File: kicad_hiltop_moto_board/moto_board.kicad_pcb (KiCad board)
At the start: 4 copper layers, 159.9 x 99.9 mm, 421 parts, among them J1 Conn_02x06_Counter_Clockwise, J10 Conn_ARM_JTAG_SWD_10, J2 Conn_02x06_Counter_Clockwise, J3 Conn_03x32_DIN41612, J4 Conn_02x06_Counter_Clockwise, J5 Conn_02x06_Counter_Clockwise, J6 Conn_02x06_Counter_Clockwise, J7 Conn_02x06_Counter_Clockwise, J8 Conn_02x06_Counter_Clockwise, J9 Conn_02x06_Counter_Clockwise, K1 HRS1KH-S, Q10 ZXMN6A07F, Q11 ZXMN6A07F, Q2 ZXMN6A07F, Q7 ZXMN6A07F, Q8 ZXMN6A07F, SW1 SW_Push, SW2 SW_DIP_x04, SW3 SW_DIP_x04, SW4 SW_DIP_x04, SW5 SW_DIP_x04, U1 INA250A4, U10 MAX31865, U11 MAX31865, U13 CP2102N-A01-GQFN24, U14 BTS4140N, U15 BTS4140N, U16 MAX4194, U17 BTS4140N, U18 BTS4140N, U19 MAX4194, U2 LD1117S33TR_SOT223, U20 MAX4194, U21 MAX4194, U22 STM32F072RBTx, U23 MAX4194, U24 MAX4194, U25 MAX4194, U26 MAX4194, U27 USB2502, U3 AT25DN512CSSHF-B, U4 AD8646, U5 AD8646, U6 LM75B, U7 AT24C02C-SSHM-T, U8 MAX31865, U9 MAX31865, Y1 50ppm 24.000MHZ, Y2 8MHZ, Y3 ABS25-32.768KHZ-6-T

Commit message: Started on moto board layout
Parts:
- removed C20, C21, C22, C25: 100nF, Capacitor_SMD:C_0603_1608Metric
- removed C23, C60, C61, C66, C67: 100nF, Capacitor_SMD:C_0402_1005Metric
- removed C26, C28, C29, C31, C32, C34, C36, C37, C39, C42, C44, C45, C47, C50, C53, C54: Ccm, Capacitor_SMD:C_0603_1608Metric
- removed C27, C30, C33, C35, C38, C43, C46, C51: Cdiff, Capacitor_SMD:C_0603_1608Metric
- removed C40, C41, C48, C49, C68, C69, C86, C87: 0.1uF, Capacitor_SMD:C_0402_1005Metric
- removed C57, C58, C63, C64: DNF, Capacitor_SMD:C_0805_2012Metric
- removed D14, D15, D16, D17, D18, D19, D20, D21, D22, D23, D24, D25: BAV99, Package_TO_SOT_SMD:SOT-23
- removed D4: BAT54T1G, Diode_SMD:D_SOD-123
- removed J10: Conn_ARM_JTAG_SWD_10, Connector_PinHeader_2.54mm:PinHeader_2x05_P2.54mm_Vertical
- removed J6, J7, J8, J9: Conn_02x06_Counter_Clockwise, Devtank_PCB_Lib:Molex2x06
- removed K1: HRS1KH-S, Devtank_PCB_Lib:Relay_SPDT_HRS1KH-S
- removed L3, L4, L6, L7: 2A/0.05DCR, Inductor_SMD:L_0805_2012Metric
- removed Q10, Q11: ZXMN6A07F, Package_TO_SOT_SMD:SOT-23
- removed R100, R101, R125, R126, R127, R128, R129, R130, R131, R132, R133, R134, R135, R136, R88, R89: 1K, Resistor_SMD:R_0603_1608Metric
- removed R103, R104, R91, R92: 0R, Resistor_SMD:R_0805_2012Metric
- removed R106, R107, R94, R95: 100K, Resistor_SMD:R_0603_1608Metric
- removed R113, R117, R122, R123, R42, R43, R44, R45, R49, R51, R53, R58, R59, R60, R61, R67, R68, R70, R71: R, Resistor_SMD:R_0603_1608Metric
- removed R114, R115, R116, R118, R119, R36, R62, R63, R73: DNF, Resistor_SMD:R_0603_1608Metric
- removed R149, R41, R46, R47, R66: 0R, Resistor_SMD:R_0603_1608Metric
- removed R35: 100R, Resistor_SMD:R_0603_1608Metric
- removed R37, R38, R52: 10K, Resistor_SMD:R_0603_1608Metric
- removed R48: 2K2, Resistor_SMD:R_0603_1608Metric
- removed R50: 470R, Resistor_SMD:R_0603_1608Metric
- removed R54, R55, R64, R65: 30R, Resistor_SMD:R_0603_1608Metric
- removed R56, R57, R69, R72: 12.4K, Resistor_SMD:R_0603_1608Metric
- removed R85, R86, R97, R98: DNF, Resistor_SMD:R_0805_2012Metric
- removed SW2, SW3, SW4, SW5: SW_DIP_x04, Button_Switch_SMD:SW_DIP_SPSTx04_Slide_Copal_CHS-04B_W7.62mm_P1.27mm
- removed TP100, TP106, TP107, TP24, TP25, TP26, TP27, TP28, TP29, TP30, TP37, TP38, TP39, TP40, TP41, TP42, TP43, TP44, TP45, TP46, TP47, TP48, TP49, TP50, TP51, TP52, TP53, TP54, TP55, TP56, TP57, TP58, TP59, TP60, TP61, TP62, TP63, TP64, TP65, TP66, TP67, TP68, TP69, TP70, TP71, TP72, TP73, TP74, TP75, TP76, TP77, TP78, TP79, TP80, TP81, TP82, TP83, TP84, TP85, TP86, TP87, TP88, TP89, TP90, TP91, TP92, TP93, TP94, TP95, TP96, TP97, TP98, TP99: Test_Point, TestPoint:TestPoint_THTPad_D1.0mm_Drill0.5mm
- removed U10, U11, U8, U9: MAX31865, Package_DFN_QFN:TQFN-20-1EP_5x5mm_P0.65mm_EP3.1x3.1mm
- removed U14, U15, U17, U18: BTS4140N, Package_TO_SOT_SMD:SOT-223
- removed U16, U19, U20, U21, U23, U24, U25, U26: MAX4194, Package_SO:SOIC-8_3.9x4.9mm_P1.27mm
- removed U4, U5: AD8646, Package_SO:SOIC-8_3.9x4.9mm_P1.27mm
- removed U6: LM75B, Package_SO:SOIC-8_3.9x4.9mm_P1.27mm
- added F2: Polyfuse, Fuse:Fuse_2920_7451Metric, F.Cu at (4.80, 83.9)
- added Q1: CSD18540Q5B, Package_SON:VSONP-8-1EP_5x6_P1.27mm, F.Cu at (-28.4, 46.6)
- added Q3: CSD18540Q5B, Package_SON:VSONP-8-1EP_5x6_P1.27mm, F.Cu at (-20.6, 46.6)
- added Q4: CSD18540Q5B, Package_SON:VSONP-8-1EP_5x6_P1.27mm, F.Cu at (-20.6, 53.1)
- added Q5: CSD18540Q5B, Package_SON:VSONP-8-1EP_5x6_P1.27mm, F.Cu at (-12.7, 46.6)
- added Q6: CSD18540Q5B, Package_SON:VSONP-8-1EP_5x6_P1.27mm, F.Cu at (-12.7, 53.1)
- C1: value 100n -> 1uF; footprint Capacitor_SMD:C_0603_1608Metric -> Capacitor_SMD:C_0402_1005Metric
- C101, C94, C95, C96, C97, C98, C99: value 0.1uf -> 0.1uF
- C14, C15, C9: value 100nF -> 100uF; footprint Capacitor_SMD:C_0402_1005Metric -> Capacitor_SMD:CP_Elec_6.3x7.7
- C16, C17, C18, C19: value 100n -> 100uF; footprint Capacitor_SMD:C_0402_1005Metric -> Capacitor_SMD:CP_Elec_6.3x7.7
- C2, C6: value 100n -> 0.1uF
- C3, C7: value 100n -> 0.1uF; footprint Capacitor_SMD:C_0603_1608Metric -> Capacitor_SMD:C_0402_1005Metric
- C4: value 100n -> 0.01uF
- C5: value 100n -> 1uF
- C8: value 100n -> 100uF; footprint Capacitor_SMD:C_0603_1608Metric -> Capacitor_SMD:CP_Elec_6.3x7.7
- D2: value GRN -> LED
- F1: footprint Resistor_SMD:R_1206_3216Metric -> Fuse:Fuse_2920_7451Metric
- J1: value Conn_02x06_Counter_Clockwise -> Conn_01x04; footprint Devtank_PCB_Lib:Molex2x06 -> Connector_TE-Connectivity:TE_MATE-N-LOK_350211-1_1x04_P5.08mm_Vertical
- J2, J4: value Conn_02x06_Counter_Clockwise -> Conn_01x04
- J5: value Conn_02x06_Counter_Clockwise -> Conn_02x05_Top_Bottom; footprint Devtank_PCB_Lib:Molex2x06 -> Connector_PinHeader_2.54mm:PinHeader_2x05_P2.54mm_Vertical
- Q2, Q7, Q8: value ZXMN6A07F -> CSD18540Q5B; footprint Package_TO_SOT_SMD:SOT-23 -> Package_SON:VSONP-8-1EP_5x6_P1.27mm
- R1: value 470 -> DNF; footprint Resistor_SMD:R_0603_1608Metric -> Resistor_SMD:R_0805_2012Metric
- R10, R11: footprint Resistor_SMD:R_1206_3216Metric -> Resistor_SMD:R_0603_1608Metric
- R12, R3, R4, R7: value 10k -> 0R
- R13: value R -> 0R; footprint Resistor_SMD:R_0603_1608Metric -> Resistor_SMD:R_0805_2012Metric
- R19: value 16K -> 10K
- R2, R5, R6: value 470 -> 0R
- R21, R24, R26: value 10K -> 0R
- R22: value 16K -> 200R
- R23: value 100R -> 10K
- R25, R27: value 16K -> 0R
- R28: value 100R -> 0R
- R29: value 100R -> 0.5R
- R30, R32: value 0R -> 0.5R
- R31: value DNF -> 0.5R
- R33: value DNF -> 0R
- R8, R9: value DNF -> 0R; footprint Resistor_SMD:R_1206_3216Metric -> Resistor_SMD:R_0603_1608Metric
- U1: value INA250A4 -> DRV8704; footprint Package_SO:TSSOP-16_4.4x5mm_P0.65mm -> Devtank_PCB_Lib:DRV8704
- moved R8 225.6 mm to (-29.7, 127.2), turned to 0 degrees
- moved Q2 224.6 mm to (-28.4, 53.1), turned to 0 degrees
- moved R10 221.2 mm to (-25.3, 124.3), turned to 0 degrees
- moved U1 219.9 mm to (-26.5, 77.9)
- moved C9 215.9 mm to (-16.8, 76.4), turned to 0 degrees
- moved R9 213.8 mm to (-17.6, 124.3), turned to 0 degrees
- moved TP8 206.2 mm to (-13.9, 119.5)
- moved D2 204.3 mm to (-19.2, 98.0)
- moved F1 203.7 mm to (-5.65, 92.1)
- moved R11 202.5 mm to (-21.7, 126.8)
- moved J4 200.8 mm to (-23.5, 119.0), turned to 0 degrees
- moved R33 193.7 mm to (-4.76, 96.8)
- moved R34 192.8 mm to (-7.15, 99.4)
- moved R13 187.6 mm to (-13.2, 116.5), turned to 0 degrees
- moved TP1 186.5 mm to (10.1, 119.4)
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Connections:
- C1 pad 1: /RTD3_R- -> GND
- C1 pad 2: /RTD3_R+ -> Net-(C1-Pad2)
- C14 pad 1: GND -> /motor_control/VM
- C14 pad 2: +5V -> GND
- C15 pad 1: GND -> /motor_control/VM
- C15 pad 2: +5V -> GND
- C16 pad 1: +3V3 -> /motor_control/VM
- C17 pad 1: +3V3 -> /motor_control/VM
- C18 pad 1: +3V3 -> /motor_control/VM
- C19 pad 1: +3V3 -> /motor_control/VM
- C2 pad 1: +3V3 -> /motor_control/V5
- C3 pad 1: /RTD1_R- -> Net-(C3-Pad1)
- C3 pad 2: /RTD1_R+ -> Net-(C3-Pad2)
- C4 pad 1: +3V3 -> GND
- C4 pad 2: GND -> /motor_control/VM
- C5 pad 1: +3V3 -> /motor_control/VM
- C5 pad 2: GND -> Net-(C5-Pad2)
- C6 pad 1: +3V3 -> /motor_control/VM
- C7 pad 1: /RTD4_R- -> /motor_control/VM
- C7 pad 2: /RTD4_R+ -> GND
- C8 pad 1: /RTD2_R- -> /motor_control/VM
- C8 pad 2: /RTD2_R+ -> GND
- C9 pad 1: +3V3 -> /motor_control/VM
- D2 pad 1: +5V -> /motor_control/FAULTn
- F1 pad 1: Net-(F1-Pad1) -> (no net)
- F1 pad 2: Net-(F1-Pad2) -> /motor_control/VM
- J1 pad 1: /GPIO5 -> /12V_EXT
- J1 pad 2: /GPIO6 -> GND
- J1 pad 3: /GPIO7 -> (no net)
- J1 pad 4: /GPIO8 -> (no net)
- J2 pad 1: (no net) -> /BOUT1
- J2 pad 10: /GPIO10 -> (no net)
- J2 pad 11: /GPIO11 -> (no net)
- J2 pad 12: /GPIO12 -> (no net)
- J2 pad 2: GND -> /BOUT2
- J2 pad 3: (no net) -> GND
- J2 pad 4: GND -> (no net)
- J2 pad 5: GND -> (no net)
- J2 pad 6: /HS_OUT4 -> (no net)
- J2 pad 7: /HS_OUT3 -> (no net)
- J2 pad 8: GND -> (no net)
- J2 pad 9: /GPIO9 -> (no net)
- J4 pad 1: /TH1+ -> /AOUT1
- J4 pad 10: GND -> (no net)
- J4 pad 11: /TH2- -> (no net)
- J4 pad 12: /TH2+ -> (no net)
- J4 pad 2: /TH1- -> /AOUT2
- J4 pad 4: GND -> (no net)
- J4 pad 5: /TH3+ -> (no net)
- J4 pad 6: /TH3- -> (no net)
- J4 pad 7: /TH4- -> (no net)
- J4 pad 8: /TH4+ -> (no net)
- J4 pad 9: GND -> (no net)
- J5 pad 1: (no net) -> +3V3
- J5 pad 10: /ADC13 -> /STM_RESET
- J5 pad 2: (no net) -> /SWD_IO
- J5 pad 3: (no net) -> GND
- J5 pad 4: (no net) -> /SWD_SCK
- J5 pad 6: /ADC6 -> (no net)
- J5 pad 7: GND -> (no net)
- J5 pad 8: /ADC12 -> (no net)
- Q2 pad 2: GND -> (no net)
- Q2 pad 3: Net-(D4-Pad2) -> /BOUT1
- Q7 pad 2: GND -> (no net)
- Q7 pad 3: Net-(Q7-Pad3) -> Net-(Q4-Pad3)
- Q8 pad 2: GND -> (no net)
- Q8 pad 3: Net-(Q8-Pad3) -> Net-(Q6-Pad3)
- R1 pad 1: Net-(R1-Pad1) -> ADJ_DC
- R1 pad 2: Net-(R1-Pad2) -> /motor_control/VM
- R10 pad 1: Net-(F1-Pad2) -> /motor_control/SCS
- R10 pad 2: +12V -> /M_SCS
- R11 pad 1: /OUT1_COM -> /motor_control/SDATO
- R11 pad 2: Net-(R11-Pad2) -> /M_SDATO
- R12 pad 1: +3V3 -> /motor_control/FAULTn
- R12 pad 2: /GPIO4 -> /M_FAULTn
- R13 pad 1: Net-(C34-Pad2) -> /12V_EXT
- R13 pad 2: /F1+ -> /motor_control/VM
- R18 pad 1: Net-(R18-Pad1) -> /motor_control/SDATO
- R18 pad 2: /5V_ADC9 -> +3V3
- R19 pad 1: GND -> /motor_control/FAULTn
- R19 pad 2: Net-(R18-Pad1) -> /motor_control/V5
- R2 pad 1: Net-(R2-Pad1) -> /motor_control/SLEEPn
- R2 pad 2: Net-(R2-Pad2) -> /M_SLEEPn
- R21 pad 2: /5V_ADC11 -> (no net)
- R22 pad 1: GND -> /motor_control/V5
- R22 pad 2: Net-(R21-Pad1) -> Net-(D2-Pad2)
- R23 pad 1: /ADC12 -> /motor_control/SCS
- R23 pad 2: Net-(R23-Pad2) -> +3V3
- R24 pad 2: /5V_ADC10 -> (no net)
- R25 pad 1: GND -> Net-(R25-Pad1)
- R25 pad 2: Net-(R24-Pad1) -> (no net)
- R26 pad 2: /5V_ADC12 -> (no net)
- R27 pad 1: GND -> Net-(R27-Pad1)
- R27 pad 2: Net-(R26-Pad1) -> (no net)
- R28 pad 1: /ADC13 -> Net-(R28-Pad1)
- R28 pad 2: Net-(R28-Pad2) -> (no net)
- R29 pad 1: /ADC6 -> GND
- R29 pad 2: Net-(R29-Pad2) -> Net-(Q4-Pad3)
- R3 pad 1: +3V3 -> /motor_control/RESET
- R3 pad 2: /GPIO6 -> /M_RESET
- R30 pad 1: +3V3 -> GND
- R30 pad 2: Net-(R30-Pad2) -> Net-(Q4-Pad3)
- R31 pad 1: Net-(R30-Pad2) -> GND
- R31 pad 2: GND -> Net-(Q6-Pad3)
- R32 pad 1: +3V3 -> GND
- R32 pad 2: Net-(R32-Pad2) -> Net-(Q6-Pad3)
- R33 pad 1: Net-(R32-Pad2) -> Net-(R33-Pad1)
- R33 pad 2: GND -> (no net)
- R34 pad 1: +3V3 -> Net-(R34-Pad1)
- R34 pad 2: Net-(R34-Pad2) -> (no net)
- R4 pad 1: +3V3 -> /motor_control/AIN1
- R4 pad 2: /GPIO2 -> /M_AIN1
- R40 pad 1: /SWD_IO -> +3V3
- R40 pad 2: +3V3 -> /SWD_IO
- R5 pad 1: Net-(R5-Pad1) -> /motor_control/AIN2
- R5 pad 2: Net-(R5-Pad2) -> /M_AIN2
- R6 pad 1: Net-(R6-Pad1) -> /motor_control/BIN1
- R6 pad 2: Net-(R6-Pad2) -> /M_BIN1
- R7 pad 1: +3V3 -> /motor_control/BIN2
- R7 pad 2: /GPIO8 -> /M_BIN2
- R8 pad 1: Net-(F1-Pad2) -> /motor_control/SCLK
- R8 pad 2: +3V3 -> /M_SCLK
- R9 pad 1: Net-(F1-Pad2) -> /motor_control/SDATI
- R9 pad 2: ADJ_DC -> /M_SDATI
- TP1 pad 1: /TH1+ -> /M_SLEEPn
- TP10 pad 1: /TH3+ -> /M_SCS
- TP11 pad 1: /TH3- -> /M_SDATO
- TP12 pad 1: /TH4+ -> /12V_EXT
- TP13 pad 1: /GPIO1_EXT -> /AOUT1
- TP14 pad 1: /GPIO2_EXT -> /AOUT2
- TP15 pad 1: /GPIO3_EXT -> /BOUT1
- TP16 pad 1: /GPIO4_EXT -> /BOUT2
- TP17 pad 1: /GPIO5_EXT -> Net-(Q4-Pad3)
- TP18 pad 1: /GPIO6_EXT -> Net-(Q6-Pad3)
- TP19 pad 1: /GPIO7_EXT -> GND
- TP20 pad 1: /GPIO8_EXT -> GND
- TP21 pad 1: /GPIO9_EXT -> /motor_control/VM
- TP22 pad 1: /GPIO10_EXT -> /motor_control/VM
- TP23 pad 1: /GPIO11_EXT -> /M_FAULTn
- TP3 pad 1: /5V_ADC9 -> /M_RESET
- TP4 pad 1: /5V_ADC10 -> /M_AIN1
- TP5 pad 1: /5V_ADC11 -> /M_AIN2
- TP6 pad 1: /5V_ADC12 -> /M_BIN1
- TP7 pad 1: /TH1- -> /M_BIN2
- TP8 pad 1: /TH2+ -> /M_SCLK
- TP9 pad 1: /TH2- -> /M_SDATI
- U1 pad 1: Net-(R11-Pad2) -> Net-(C3-Pad1)
- U1 pad 10: +3V3 -> /motor_control/AIN1
- U1 pad 11: GND -> /motor_control/AIN2
- U1 pad 12: Net-(U1-Pad12) -> /motor_control/BIN1
- U1 pad 13: Net-(U1-Pad12) -> /motor_control/BIN2
- U1 pad 14: Net-(F1-Pad1) -> /motor_control/SCLK
- U1 pad 15: Net-(F1-Pad1) -> /motor_control/SDATI
- U1 pad 16: Net-(F1-Pad1) -> /motor_control/SCS
- U1 pad 2: Net-(R11-Pad2) -> Net-(C3-Pad2)
- U1 pad 3: Net-(R11-Pad2) -> Net-(C5-Pad2)
- U1 pad 4: Net-(U1-Pad4) -> /motor_control/VM
- U1 pad 5: Net-(U1-Pad4) -> GND
- U1 pad 6: GND -> /motor_control/V5
- U1 pad 7: GND -> Net-(C1-Pad2)
- U1 pad 8: GND -> /motor_control/SLEEPn
- U1 pad 9: /I_MON -> /motor_control/RESET
- U22 pad 10: /ADC10 -> (no net)
- U22 pad 11: /ADC11 -> (no net)
- U22 pad 14: /ADC1 -> (no net)
- U22 pad 15: /GPIO12 -> (no net)
- U22 pad 16: /ADC2 -> (no net)
- U22 pad 17: /ADC3 -> (no net)
- U22 pad 2: /GPIO11 -> (no net)
- U22 pad 20: /ADC4 -> (no net)
- U22 pad 22: /ADC5 -> (no net)
- U22 pad 23: /ADC6 -> (no net)
- U22 pad 24: /ADC12 -> (no net)
- U22 pad 25: /ADC13 -> (no net)
- U22 pad 27: /ADC7 -> (no net)
- U22 pad 33: /HS_CTRL_SW2 -> (no net)
- U22 pad 34: /GPIO5 -> /M_BIN2
- U22 pad 35: /GPIO6 -> /M_SLEEPn
- U22 pad 36: /GPIO7 -> /M_RESET
- U22 pad 38: /GPIO8 -> /M_FAULTn
- U22 pad 39: /GPIO1 -> /M_SCS
- U22 pad 40: /GPIO3 -> /M_AIN2
- U22 pad 41: /GPIO2 -> /M_AIN1
- U22 pad 42: /GPIO4 -> /M_BIN1
- U22 pad 43: /HS_CTRL_SW1 -> (no net)
- U22 pad 50: /HS_CTRL_SW4 -> (no net)
- U22 pad 53: /HS_CTRL_SW3 -> (no net)
- U22 pad 54: /GPIO9 -> (no net)
- U22 pad 55: /STM_SPI1_SCK -> /M_SCLK
- U22 pad 56: /STM_SPI1_MISO -> /M_SDATO
- U22 pad 57: /STM_SPI1_MOSI -> /M_SDATI
- U22 pad 58: /STM_SCL -> (no net)
- U22 pad 59: /STM_SDA -> (no net)
- U22 pad 61: /GPIO10 -> (no net)
- U22 pad 62: /RL1_OUT -> (no net)
- U22 pad 8: /STM_Micro/ADC8 -> (no net)
- U22 pad 9: /ADC9 -> (no net)
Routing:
- net /M_FAULTn: track 0.00 -> 122.2 mm, vias 0 -> 2
- net /GPIO8: track 122.2 -> 0.00 mm, vias 2 -> 0
- net /M_RESET: track 0.00 -> 96.8 mm, vias 0 -> 1
- net /GPIO7: track 116.7 -> 19.9 mm, vias 1 -> 0
- net /STM_SPI1_SCK: track 91.8 -> 0.00 mm, vias 10 -> 0
- net /M_SCLK: track 0.00 -> 91.8 mm, vias 0 -> 10
- net /STM_SPI1_MOSI: track 87.6 -> 0.00 mm, vias 9 -> 0
- net /M_SDATI: track 0.00 -> 87.6 mm, vias 0 -> 9
- net /STM_SPI1_MISO: track 85.4 -> 0.00 mm, vias 11 -> 0
- net /M_SDATO: track 0.00 -> 85.4 mm, vias 0 -> 11
- net /M_SCS: track 0.00 -> 75.2 mm, vias 0 -> 5
- net /GPIO1: track 75.2 -> 0.00 mm, vias 5 -> 0
- net /GPIO4: track 112.9 -> 46.4 mm
- net /M_BIN1: track 0.00 -> 66.5 mm
- net /GPIO2: track 90.4 -> 32.1 mm, vias 5 -> 1
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
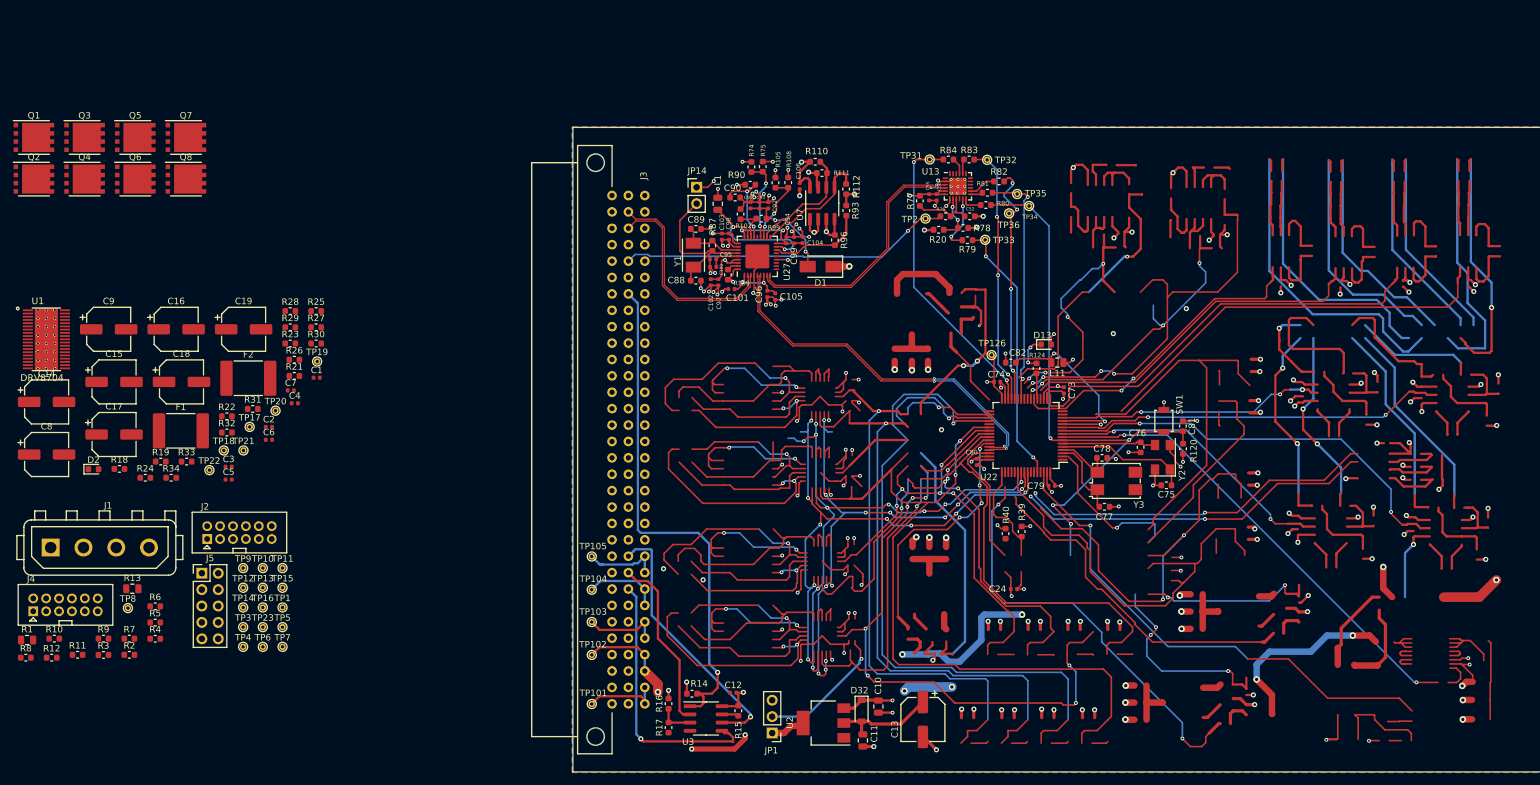
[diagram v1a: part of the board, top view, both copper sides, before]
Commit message: Rough layout of moto board
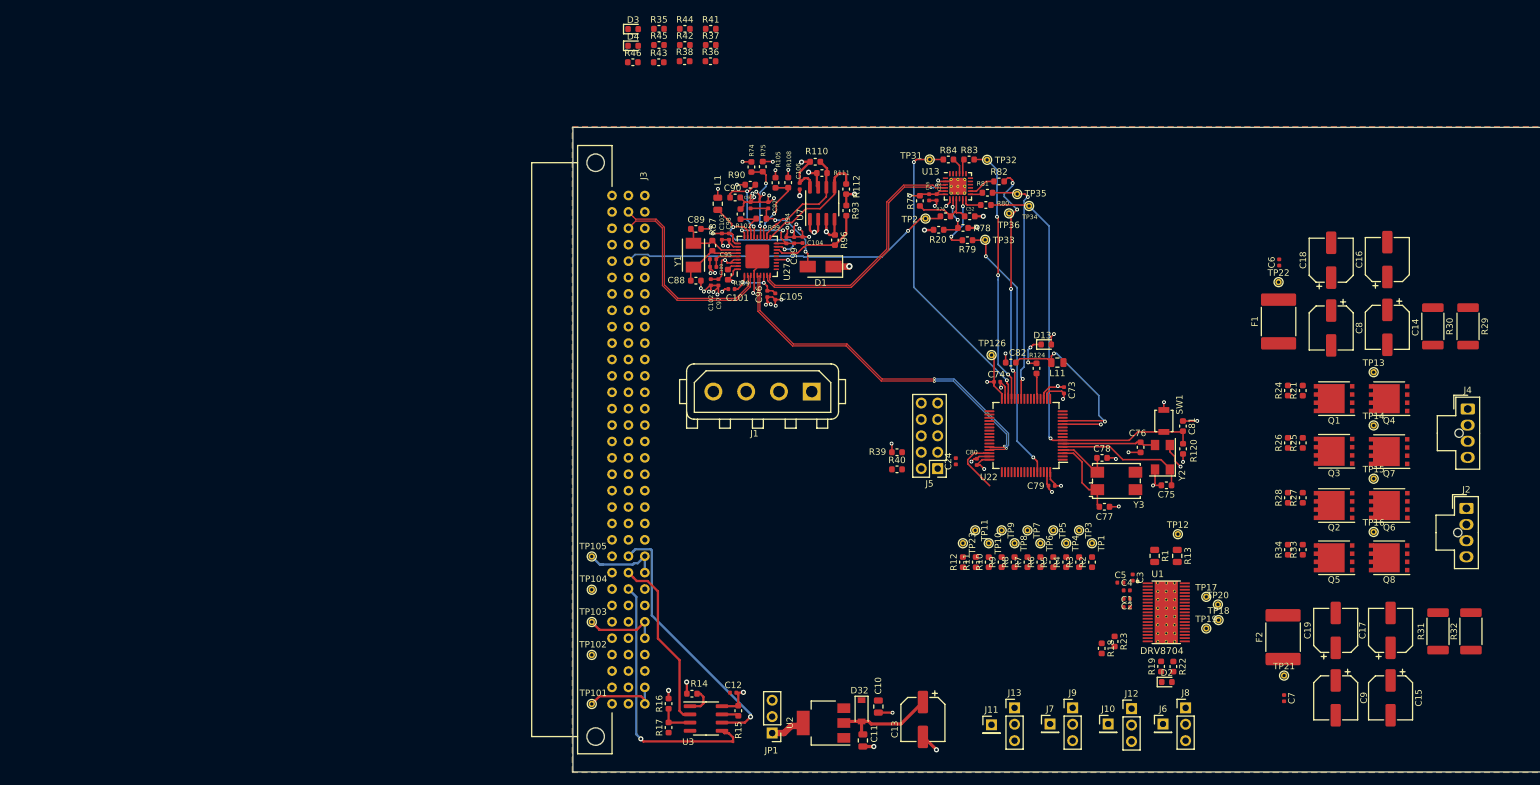
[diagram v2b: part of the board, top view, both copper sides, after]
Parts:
- removed C93: 0.1uF, Capacitor_SMD:C_0402_1005Metric
- removed JP14: DNF, Connector_PinHeader_2.54mm:PinHeader_1x02_P2.54mm_Vertical
- added D3: GRN, LED_SMD:LED_0603_1608Metric, F.Cu at (64.4, 29.8)
- added D4: GRN, LED_SMD:LED_0603_1608Metric, F.Cu at (64.4, 32.4)
- added J10: Conn_01x01, Connector_PinHeader_2.54mm:PinHeader_1x01_P2.54mm_Vertical, F.Cu at (138.0, 137.5)
- added J11: Conn_01x01, Connector_PinHeader_2.54mm:PinHeader_1x01_P2.54mm_Vertical, F.Cu at (119.9, 137.6)
- added J12: Conn_01x03, Connector_PinHeader_2.54mm:PinHeader_1x03_P2.54mm_Vertical, F.Cu at (141.6, 135.1)
- added J13: Conn_01x03, Connector_PinHeader_2.54mm:PinHeader_1x03_P2.54mm_Vertical, F.Cu at (123.5, 135.0)
- added J6: Conn_01x01, Connector_PinHeader_2.54mm:PinHeader_1x01_P2.54mm_Vertical, F.Cu at (146.5, 137.5)
- added J7: Conn_01x01, Connector_PinHeader_2.54mm:PinHeader_1x01_P2.54mm_Vertical, F.Cu at (129.0, 137.5)
- added J8: Conn_01x03, Connector_PinHeader_2.54mm:PinHeader_1x03_P2.54mm_Vertical, F.Cu at (150.0, 135.0)
- added J9: Conn_01x03, Connector_PinHeader_2.54mm:PinHeader_1x03_P2.54mm_Vertical, F.Cu at (132.5, 135.0)
- added R35: 0R, Resistor_SMD:R_0603_1608Metric, F.Cu at (68.4, 29.8)
- added R36: 0R, Resistor_SMD:R_0603_1608Metric, F.Cu at (76.4, 34.8)
- added R37: DNF, Resistor_SMD:R_0603_1608Metric, F.Cu at (76.4, 32.3)
- added R38: DNF, Resistor_SMD:R_0603_1608Metric, F.Cu at (72.4, 34.8)
- added R41: 100K, Resistor_SMD:R_0603_1608Metric, F.Cu at (76.4, 29.8)
- added R42: 100K, Resistor_SMD:R_0603_1608Metric, F.Cu at (72.4, 32.3)
- added R43: 330R, Resistor_SMD:R_0603_1608Metric, F.Cu at (68.4, 35.0)
- added R44: 330R, Resistor_SMD:R_0603_1608Metric, F.Cu at (72.4, 29.8)
- added R45: DNF, Resistor_SMD:R_0603_1608Metric, F.Cu at (68.4, 32.3)
- added R46: DNF, Resistor_SMD:R_0603_1608Metric, F.Cu at (64.4, 35.0)
- C106: value 0.1uF -> DNF
- J2, J4: footprint Devtank_PCB_Lib:Molex2x06 -> Connector_Molex:Molex_Nano-Fit_105309-xx04_1x04_P2.50mm_Vertical
- Q1, Q2, Q3, Q4, Q5, Q6, Q7, Q8: footprint Package_SON:VSONP-8-1EP_5x6_P1.27mm -> Devtank_PCB_Lib:CSD18540Q5B
- R112: value 10K -> DNF
- R29, R30, R31, R32: footprint Resistor_SMD:R_0603_1608Metric -> Resistor_SMD:R_2512_6332Metric
- U7: value AT24C02C-SSHM-T -> DNF
- moved J4 219.3 mm to (193.7, 88.7)
- moved C14 208.0 mm to (181.2, 76.0), turned to 270 degrees
- moved Q2 207.7 mm to (173.0, 103.7), turned to 180 degrees
- moved Q1 205.4 mm to (173.0, 87.1), turned to 180 degrees
- moved Q4 204.9 mm to (181.5, 87.1), turned to 180 degrees
- moved C15 203.7 mm to (181.8, 133.4), turned to 270 degrees
- moved Q6 200.7 mm to (181.6, 103.7), turned to 180 degrees
- moved C17 200.1 mm to (181.8, 123.0), turned to 90 degrees
- moved C8 200.0 mm to (172.6, 76.2), turned to 270 degrees
- moved Q3 199.6 mm to (173.0, 95.2), turned to 180 degrees
- moved C9 198.5 mm to (173.2, 133.4), turned to 270 degrees
- moved Q5 196.8 mm to (173.0, 111.8), turned to 180 degrees
- moved Q8 195.4 mm to (181.5, 111.8), turned to 180 degrees
- moved R32 195.2 mm to (194.2, 123.2), turned to 90 degrees
- moved Q7 192.6 mm to (181.5, 95.3), turned to 180 degrees
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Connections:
- net /motor_control/V5 renamed /V5
- F1 pad 1: (no net) -> Net-(F1-Pad1)
- F2 pad 2: (no net) -> Net-(F2-Pad2)
- Q4 pad 1: Net-(Q4-Pad1) -> (no net)
- Q6 pad 1: Net-(Q6-Pad1) -> (no net)
- Q7 pad 1: Net-(Q7-Pad1) -> (no net)
- Q8 pad 1: Net-(Q8-Pad1) -> (no net)
- R21 pad 2: (no net) -> Net-(Q1-Pad4)
- R24 pad 2: (no net) -> Net-(Q4-Pad4)
- R25 pad 2: (no net) -> Net-(Q3-Pad4)
- R26 pad 2: (no net) -> Net-(Q7-Pad4)
- R27 pad 2: (no net) -> Net-(Q2-Pad4)
- R28 pad 2: (no net) -> Net-(Q6-Pad4)
- R33 pad 2: (no net) -> Net-(Q5-Pad4)
- R34 pad 2: (no net) -> Net-(Q8-Pad4)
- U27 pad 11: (no net) -> Net-(R37-Pad2)
- U27 pad 12: (no net) -> Net-(R38-Pad2)
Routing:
- net +5V: track 357.1 -> 26.2 mm, vias 9 -> 2
- net +12V: track 243.6 -> 12.1 mm, vias 7 -> 0
- net ADJ_DC: track 231.4 -> 12.1 mm, vias 5 -> 0
- net GND: track 335.6 -> 132.5 mm, vias 137 -> 56
- net -5V: track 151.4 -> 11.8 mm, vias 3 -> 0
- net +3V3: track 221.2 -> 83.4 mm, vias 58 -> 21
- net /M_FAULTn: track 122.2 -> 0.00 mm, vias 2 -> 0
- net /M_RESET: track 96.8 -> 0.00 mm, vias 1 -> 0
- net /GPIO6: track 92.9 -> 0.00 mm, vias 1 -> 0
- net /GPIO3: track 91.8 -> 0.00 mm, vias 7 -> 0
- net /M_SCLK: track 91.8 -> 0.00 mm, vias 10 -> 0
- net /M_SDATI: track 87.6 -> 0.00 mm, vias 9 -> 0
- net /M_SDATO: track 85.4 -> 0.00 mm, vias 11 -> 0
- net /GPIO5: track 84.9 -> 0.00 mm, vias 1 -> 0
- net /RL1_OUT: track 77.1 -> 0.00 mm, vias 1 -> 0
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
